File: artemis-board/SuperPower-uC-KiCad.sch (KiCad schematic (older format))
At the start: 7 parts, among them J8 regulator board

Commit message: added cap to 3v3 I2c, swapped some footprints to normal...
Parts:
- JP4: DNP (none) -> DNP
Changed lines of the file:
@@
 F 2 "Jumper:SolderJumper-2_P1.3mm_Open_Pad1.0x1.5mm" H 8000 3450 50  0001 C CNN
 F 3 "~" H 8000 3450 50  0001 C CNN
+F 4 "DNP" H 8000 3450 50  0001 C CNN "DNP"
 	1    8000 3450
 	1    0    0    -1

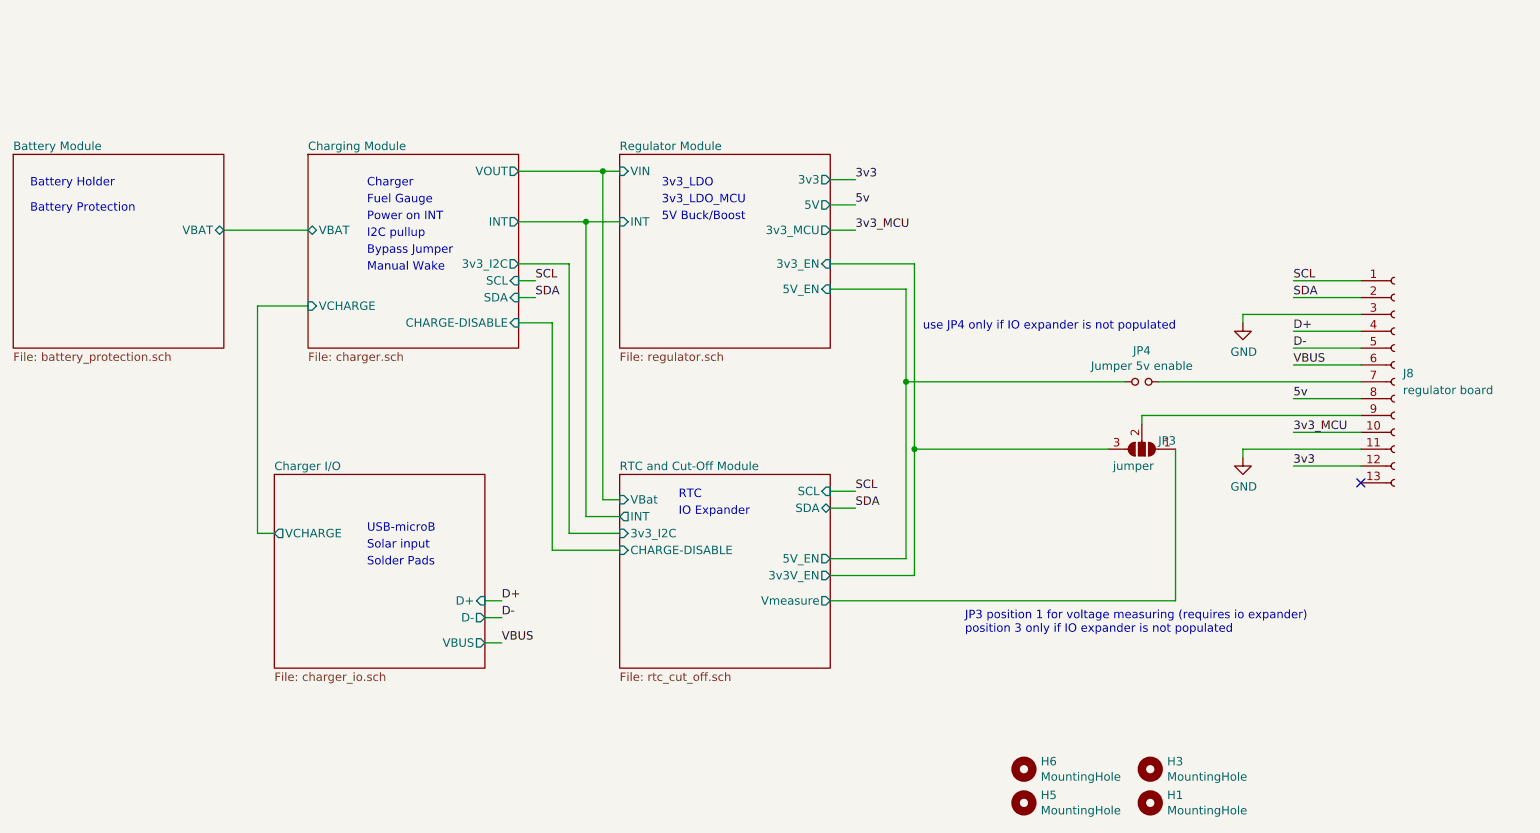
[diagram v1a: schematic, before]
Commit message: + temperature sensor, i2c header - esp voltage  measurement...
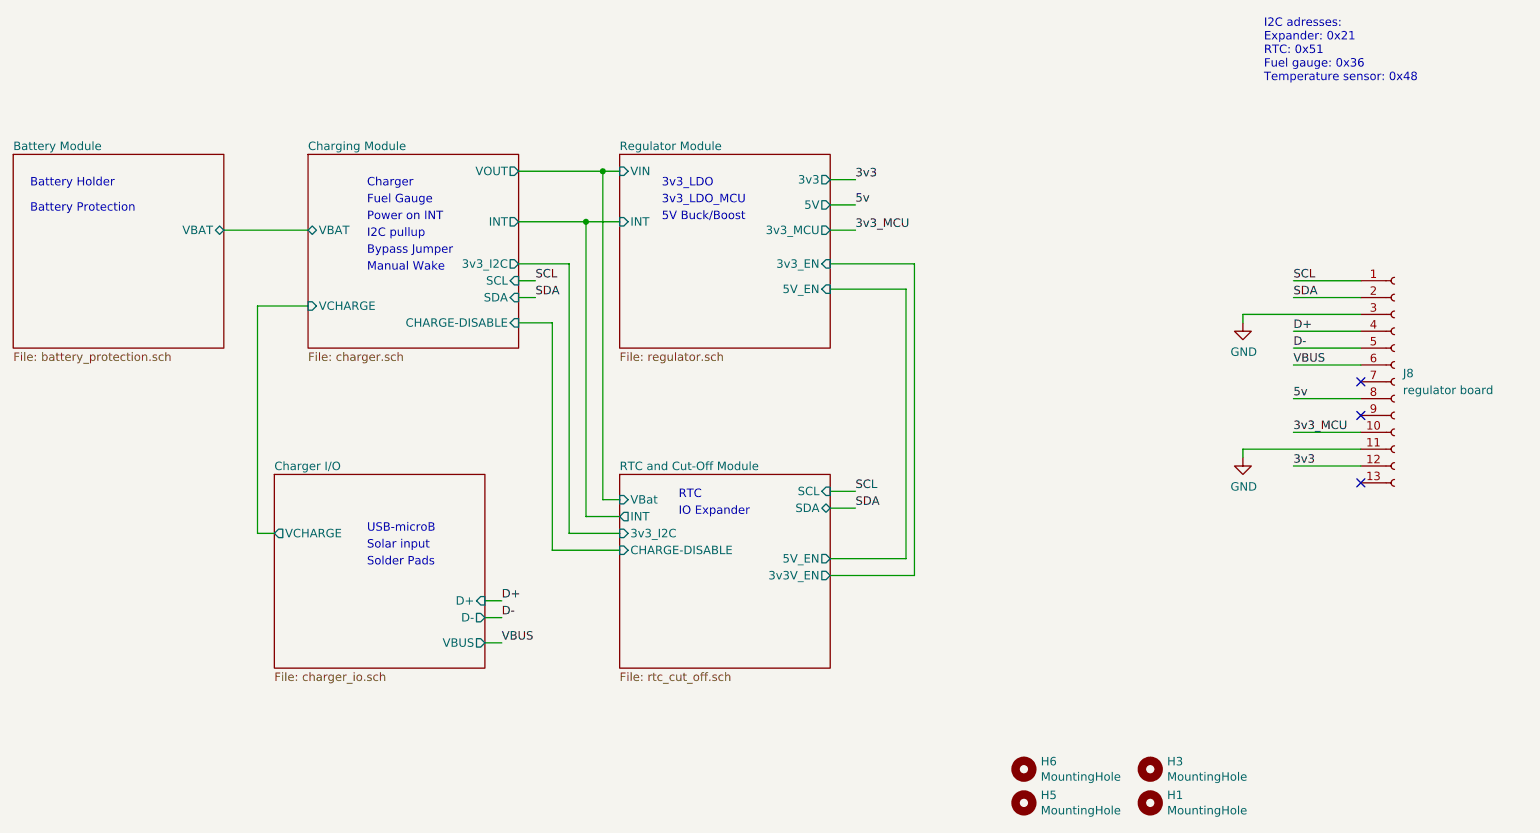
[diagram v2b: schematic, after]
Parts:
- removed JP3: jumper, Jumper:SolderJumper-3_P1.3mm_Open_Pad1.0x1.5mm, symbol Jumper:SolderJumper_3_Open
- removed JP4: Jumper 5v enable, Jumper:SolderJumper-2_P1.3mm_Open_Pad1.0x1.5mm, symbol Device:Jumper_NO_Small
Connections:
- no-connect marks 1 -> 3
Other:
- note added: "I2C adresses:\nExpander: 0x21\nRTC: 0x51\nFuel gauge: 0x36\nTemperature sensor: 0x48"
- note removed: "JP3 position 1 for voltage measuring (requires io expander)\nposition 3 only if IO expander is not populated"
- note removed: "use JP4 only if IO expander is not populated"
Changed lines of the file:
@@
 I2C pullup
 Wire Wire Line
-	6650 4600 6650 3850
-Wire Wire Line
 	6150 4600 6650 4600
 Wire Wire Line
@@
 Wire Wire Line
 	6150 2900 6600 2900
-Wire Wire Line
-	6600 2900 6600 3450
 Wire Wire Line
 	6600 4500 6150 4500
@@
 F8 "3v3_I2C" I L 4900 4350 50
 F9 "VBat" I L 4900 4150 50
-F10 "Vmeasure" O R 6150 4750 50
 $EndSheet
 $Sheet
@@
 Wire Wire Line
 	4800 2200 4900 2200
-Wire Wire Line
-	6150 4750 8200 4750
 NoConn ~ 9300 4050
-$Comp
-L Device:Jumper_NO_Small JP4
-U 1 1 60D487D3
-P 8000 3450
-F 0 "JP4" H 8000 3635 50  0000 C CNN
-F 1 "Jumper 5v enable" H 8000 3544 50  0000 C CNN
-F 2 "Jumper:SolderJumper-2_P1.3mm_Open_Pad1.0x1.5mm" H 8000 3450 50  0001 C CNN
-F 3 "~" H 8000 3450 50  0001 C CNN
-F 4 "DNP" H 8000 3450 50  0001 C CNN "DNP"
-	1    8000 3450
-	1    0    0    -1
-$EndComp
-$Comp
-L Jumper:SolderJumper_3_Open JP?
-U 1 1 60D4D872
-P 8000 3850
-AR Path="/5F63B107/60D4D872" Ref="JP?"  Part="1"
-AR Path="/60D4D872" Ref="JP3"  Part="1"
-F 0 "JP3" H 7850 3800 50  0000 C CNN
-F 1 "jumper" H 8050 3950 50  0000 C CNN
-F 2 "Jumper:SolderJumper-3_P1.3mm_Open_Pad1.0x1.5mm" H 8000 3850 50  0001 C CNN
-F 3 "~" H 8000 3850 50  0001 C CNN
-F 4 "DNP" H 8000 3850 50  0001 C CNN "DNP"
-	1    8000 3850
-	-1   0    0    1
-$EndComp
-Wire Wire Line
-	8200 3850 8200 4750
-Wire Wire Line
-	8000 3650 8000 3700
-Wire Wire Line
-	8000 3650 9300 3650
-Wire Wire Line
-	9300 3450 8100 3450
-Wire Wire Line
-	7900 3450 6600 3450
-Connection ~ 6600 3450
-Wire Wire Line
-	6600 3450 6600 4500
-Wire Wire Line
-	7800 3850 6650 3850
-Connection ~ 6650 3850
-Wire Wire Line
-	6650 3850 6650 2750
-Text Notes 6700 3150 0    50   ~ 0
-use JP4 only if IO expander is not populated
-Text Notes 6950 4950 0    50   ~ 0
-JP3 position 1 for voltage measuring (requires io expander)\nposition 3 only if IO expander is not populated
+Wire Wire Line
+	6650 2750 6650 4600
+Wire Wire Line
+	6600 2900 6600 4500
+NoConn ~ 9300 3450
+NoConn ~ 9300 3650
+Text Notes 8725 1675 0    50   ~ 0
+I2C adresses:\nExpander: 0x21\nRTC: 0x51\nFuel gauge: 0x36\nTemperature sensor: 0x48
 $EndSCHEMATC

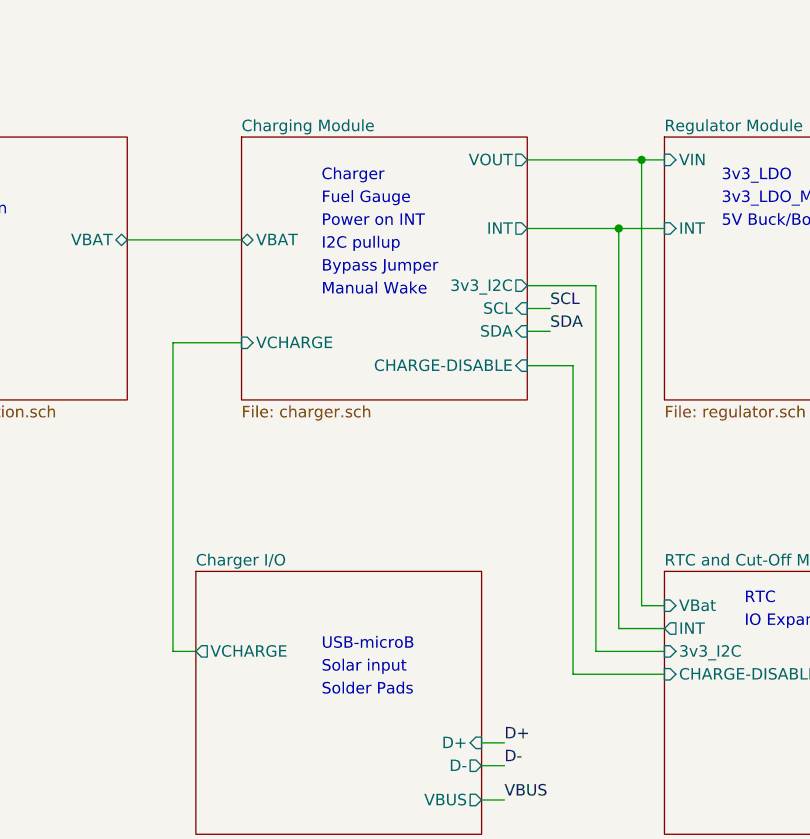
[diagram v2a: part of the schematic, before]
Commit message: added comments, part numbers and extended marker
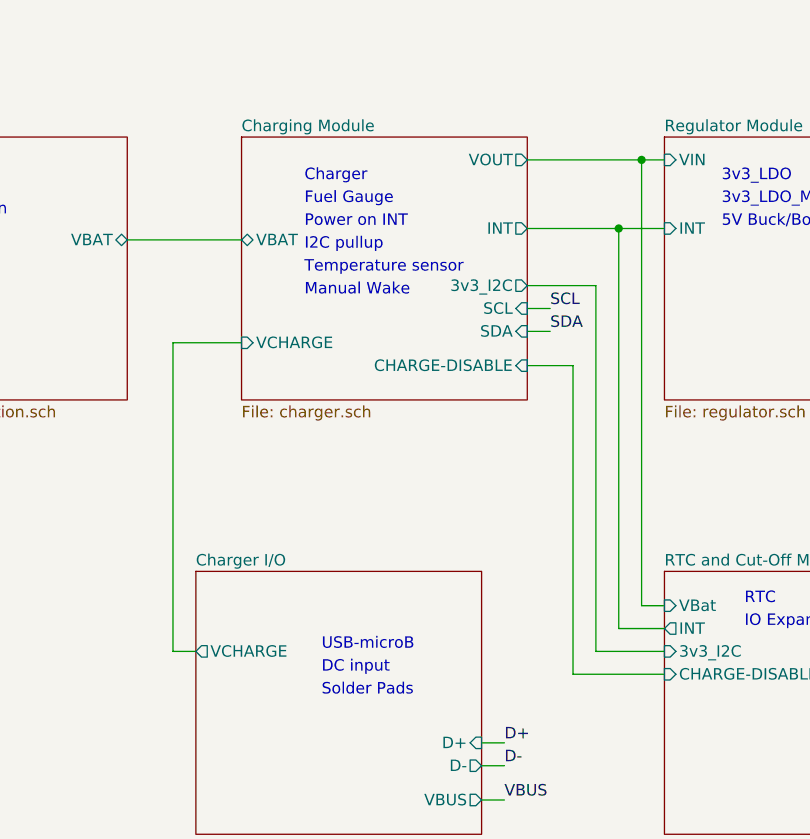
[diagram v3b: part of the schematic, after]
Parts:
- J8: Extended (none) -> Extended; LCSC C52709 -> C52709
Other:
- note added: "DC input"
- note added: "Temperature sensor"
- note removed: "Bypass Jumper"
- note removed: "Solar input"
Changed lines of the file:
@@
 Text Notes 1400 2450 0    50   ~ 0
 Battery Protection
-Text Notes 3400 2300 0    50   ~ 0
+Text Notes 3325 2300 0    50   ~ 0
 Charger
-Text Notes 3400 2400 0    50   ~ 0
+Text Notes 3325 2400 0    50   ~ 0
 Fuel Gauge
 Text Notes 5150 2300 0    50   ~ 0
@@
 USB-microB
 Text Notes 3400 4450 0    50   ~ 0
-Solar input
+DC input
 Text Notes 3400 4550 0    50   ~ 0
 Solder Pads
-Text Notes 3400 2800 0    50   ~ 0
+Text Notes 3325 2800 0    50   ~ 0
 Manual Wake
-Text Notes 3400 2700 0    50   ~ 0
-Bypass Jumper
-Text Notes 3400 2500 0    50   ~ 0
+Text Notes 3325 2500 0    50   ~ 0
 Power on INT
 Text Notes 5250 4250 0    50   ~ 0
 IO Expander
-Text Notes 3400 2600 0    50   ~ 0
+Text Notes 3325 2600 0    50   ~ 0
 I2C pullup
 Wire Wire Line
@@
 F 2 "Connector_PinSocket_2.54mm:PinSocket_1x13_P2.54mm_Vertical" H 9500 3450 50  0001 C CNN
 F 3 "~" H 9500 3450 50  0001 C CNN
-F 4 "C52709 " H 9500 3450 50  0001 C CNN "LCSC"
+F 4 "C52709" H 9500 3450 50  0001 C CNN "LCSC"
+F 5 "Extended" H 9500 3450 50  0001 C CNN "Extended"
 	1    9500 3450
 	1    0    0    -1
@@
 Text Notes 8725 1675 0    50   ~ 0
 I2C adresses:\nExpander: 0x21\nRTC: 0x51\nFuel gauge: 0x36\nTemperature sensor: 0x48
+Text Notes 3325 2700 0    50   ~ 0
+Temperature sensor
 $EndSCHEMATC
